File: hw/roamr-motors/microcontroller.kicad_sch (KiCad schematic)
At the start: 38 parts, among them J1 USB_C_Receptacle_USB2.0_14P, J2 USB_C_Receptacle_USB2.0_14P, Q1 L8050QLT1G, Q2 QL8050QLT1G, SW1 SW_MEC_5G, SW2 SW_MEC_5G, U3 ESP32-S3-WROOM-1, U4 CP2102N-A02-GQFN28

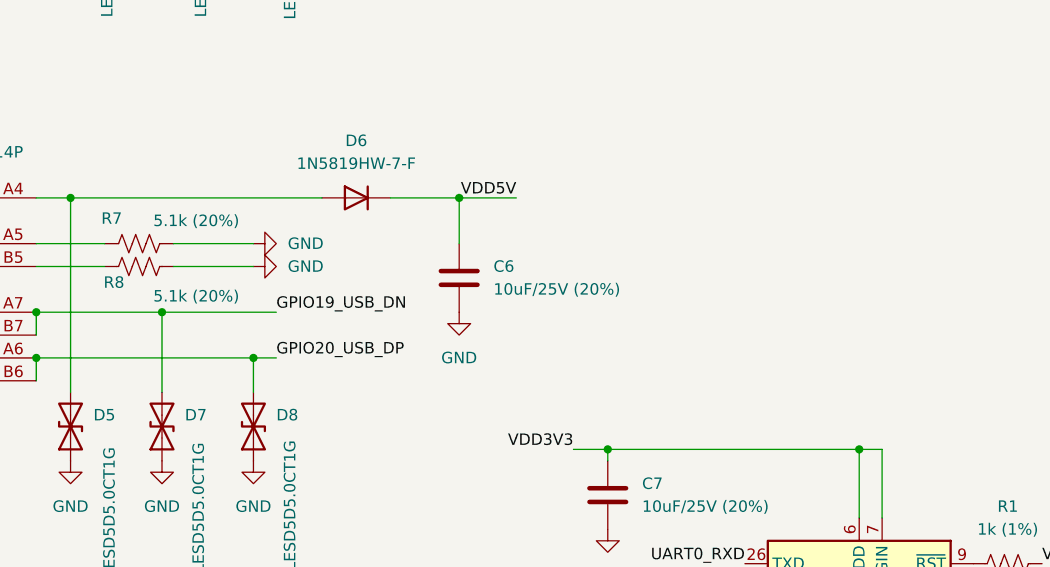
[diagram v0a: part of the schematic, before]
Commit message: Add series resistors
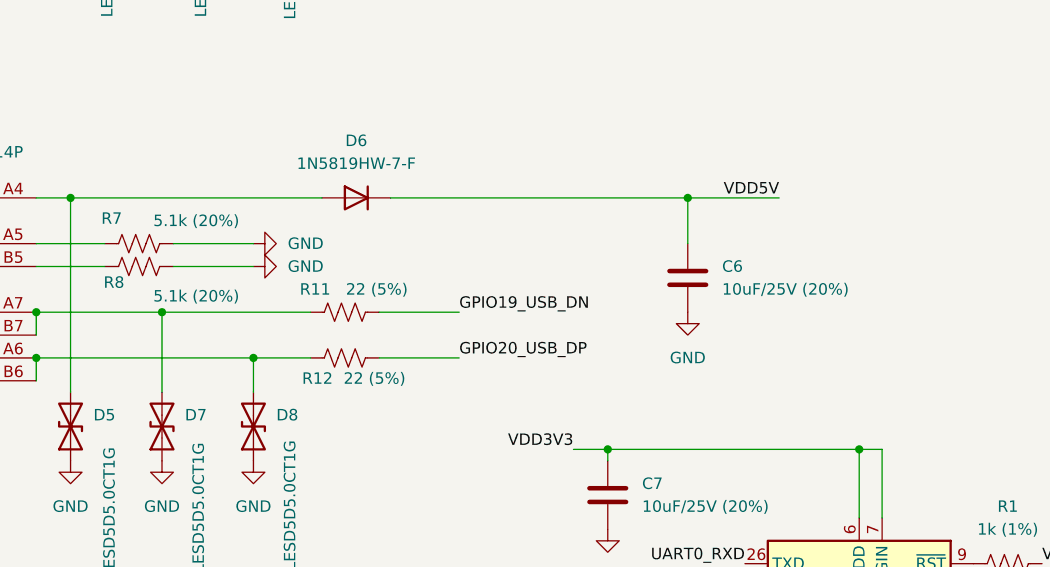
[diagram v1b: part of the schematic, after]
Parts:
- added R11, R12: 22 (5%), symbol Device:R_US
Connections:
- net GPIO19_USB_DN: now also R11.2; no longer D7.2 (A2), J2.A7 (D-), J2.B7 (D-)
- net GPIO20_USB_DP: now also R12.2; no longer D8.2 (A2), J2.A6 (D+), J2.B6 (D+)
- new net: D8.2 (A2), J2.A6 (D+), J2.B6 (D+), R12.1
- new net: D7.2 (A2), J2.A7 (D-), J2.B7 (D-), R11.1
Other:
- moved on the sheet: C6
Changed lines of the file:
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@@
 	)
 	(junction
-		(at 71.12 102.87)
-		(diameter 0)
-		(color 0 0 0 0)
-	)
-	(junction
 		(at 170.18 138.43)
 		(diameter 0)
@@
 	)
 	(junction
-		(at 60.96 97.79)
-		(diameter 0)
-		(color 0 0 0 0)
-	)
-	(junction
-		(at 93.98 85.09)
-		(diameter 0)
-		(color 0 0 0 0)
-	)
-	(junction
 		(at 71.12 41.91)
 		(diameter 0)
@@
 	)
 	(junction
+		(at 60.96 97.79)
+		(diameter 0)
+		(color 0 0 0 0)
+	)
+	(junction
 		(at 50.8 24.13)
 		(diameter 0)
@@
 		(color 0 0 0 0)
 	)
+	(junction
+		(at 119.38 85.09)
+		(diameter 0)
+		(color 0 0 0 0)
+	)
+	(junction
+		(at 71.12 102.87)
+		(diameter 0)
+		(color 0 0 0 0)
+	)
 	(no_connect
 		(at 125.73 181.61)
@@
 	(wire
 		(pts
-			(xy 71.12 102.87) (xy 73.66 102.87)
-		)
-		(stroke
-			(width 0)
-			(type default)
-		)
-	)
-	(wire
-		(pts
 			(xy 46.99 97.79) (xy 46.99 100.33)
 		)
@@
 	(wire
 		(pts
-			(xy 100.33 85.09) (xy 93.98 85.09)
-		)
-		(stroke
-			(width 0)
-			(type default)
-		)
-	)
-	(wire
-		(pts
 			(xy 187.96 138.43) (xy 196.85 138.43)
 		)
@@
 	(wire
 		(pts
+			(xy 86.36 85.09) (xy 119.38 85.09)
+		)
+		(stroke
+			(width 0)
+			(type default)
+		)
+	)
+	(wire
+		(pts
+			(xy 85.09 97.79) (xy 93.98 97.79)
+		)
+		(stroke
+			(width 0)
+			(type default)
+		)
+	)
+	(wire
+		(pts
 			(xy 119.38 26.67) (xy 121.92 26.67)
 		)
@@
 	(wire
 		(pts
-			(xy 100.33 24.13) (xy 93.98 24.13)
+			(xy 71.12 102.87) (xy 77.47 102.87)
 		)
 		(stroke
@@
 	(wire
 		(pts
-			(xy 60.96 97.79) (xy 73.66 97.79)
+			(xy 100.33 24.13) (xy 93.98 24.13)
 		)
 		(stroke
@@
 	(wire
 		(pts
+			(xy 85.09 102.87) (xy 93.98 102.87)
+		)
+		(stroke
+			(width 0)
+			(type default)
+		)
+	)
+	(wire
+		(pts
 			(xy 170.18 138.43) (xy 187.96 138.43)
 		)
@@
 	(wire
 		(pts
-			(xy 86.36 85.09) (xy 93.98 85.09)
+			(xy 200.66 104.14) (xy 205.74 104.14)
 		)
 		(stroke
@@
 	(wire
 		(pts
-			(xy 200.66 104.14) (xy 205.74 104.14)
+			(xy 60.96 97.79) (xy 77.47 97.79)
 		)
 		(stroke
@@
 	(wire
 		(pts
+			(xy 129.54 85.09) (xy 119.38 85.09)
+		)
+		(stroke
+			(width 0)
+			(type default)
+		)
+	)
+	(wire
+		(pts
 			(xy 140.97 113.03) (xy 140.97 120.65)
 		)
@@
 	(wire
 		(pts
-			(xy 93.98 90.17) (xy 93.98 85.09)
+			(xy 119.38 90.17) (xy 119.38 85.09)
 		)
 		(stroke
@@
 	)
 	(label "GPIO19_USB_DN"
-		(at 73.66 97.79 0)
+		(at 93.98 97.79 0)
 		(effects
 			(font
@@
 	)
 	(label "VDD5V"
-		(at 100.33 85.09 180)
+		(at 129.54 85.09 180)
 		(effects
 			(font
@@
 	)
 	(label "GPIO20_USB_DP"
-		(at 73.66 102.87 0)
+		(at 93.98 102.87 0)
 		(effects
 			(font
@@
 	)
 	(symbol
+		(lib_id "Device:R_US")
+		(at 81.28 102.87 90)
+		(unit 1)
+		(exclude_from_sim no)
+		(in_bom yes)
+		(on_board yes)
+		(dnp no)
+		(property "Reference" "R12"
+			(at 78.232 105.156 90)
+			(effects
+				(font
+					(size 1.27 1.27)
+				)
+			)
+		)
+		(property "Value" "22 (5%)"
+			(at 84.582 105.156 90)
+			(effects
+				(font
+					(size 1.27 1.27)
+				)
+			)
+		)
+		(property "Footprint" ""
+			(at 81.534 101.854 90)
+			(effects
+				(font
+					(size 1.27 1.27)
+				)
+				(hide yes)
+			)
+		)
+		(property "Datasheet" "~"
+			(at 81.28 102.87 0)
+			(effects
+				(font
+					(size 1.27 1.27)
+				)
+				(hide yes)
+			)
+		)
+		(property "Description" "Resistor, US symbol"
+			(at 81.28 102.87 0)
+			(effects
+				(font
+					(size 1.27 1.27)
+				)
+				(hide yes)
+			)
+		)
+		(pin "2"
+		)
+		(pin "1"
+		)
+		(instances
+			(project "roamr-motors"
+				(path "/db664d1d-d972-4e66-af85-94b6971e1c6e/206ea9a6-1e38-4e76-a070-d60887d5750e"
+					(reference "R12")
+					(unit 1)
+				)
+			)
+		)
+	)
+	(symbol
+		(lib_id "Device:R_US")
+		(at 81.28 97.79 90)
+		(unit 1)
+		(exclude_from_sim no)
+		(in_bom yes)
+		(on_board yes)
+		(dnp no)
+		(property "Reference" "R11"
+			(at 77.978 95.25 90)
+			(effects
+				(font
+					(size 1.27 1.27)
+				)
+			)
+		)
+		(property "Value" "22 (5%)"
+			(at 84.836 95.25 90)
+			(effects
+				(font
+					(size 1.27 1.27)
+				)
+			)
+		)
+		(property "Footprint" ""
+			(at 81.534 96.774 90)
+			(effects
+				(font
+					(size 1.27 1.27)
+				)
+				(hide yes)
+			)
+		)
+		(property "Datasheet" "~"
+			(at 81.28 97.79 0)
+			(effects
+				(font
+					(size 1.27 1.27)
+				)
+				(hide yes)
+			)
+		)
+		(property "Description" "Resistor, US symbol"
+			(at 81.28 97.79 0)
+			(effects
+				(font
+					(size 1.27 1.27)
+				)
+				(hide yes)
+			)
+		)
+		(pin "1"
+		)
+		(pin "2"
+		)
+		(instances
+			(project "roamr-motors"
+				(path "/db664d1d-d972-4e66-af85-94b6971e1c6e/206ea9a6-1e38-4e76-a070-d60887d5750e"
+					(reference "R11")
+					(unit 1)
+				)
+			)
+		)
+	)
+	(symbol
 		(lib_id "power:GND")
 		(at 60.96 53.34 0)
@@
 	(symbol
 		(lib_id "power:GND")
-		(at 93.98 97.79 0)
+		(at 119.38 97.79 0)
 		(unit 1)
 		(exclude_from_sim no)
@@
 		(fields_autoplaced yes)
 		(property "Reference" "#PWR015"
-			(at 93.98 104.14 0)
+			(at 119.38 104.14 0)
 			(effects
 				(font
@@
 		)
 		(property "Value" "GND"
-			(at 93.98 102.87 0)
+			(at 119.38 102.87 0)
 			(effects
 				(font
@@
 		)
 		(property "Footprint" ""
-			(at 93.98 97.79 0)
+			(at 119.38 97.79 0)
 			(effects
 				(font
@@
 		)
 		(property "Datasheet" ""
-			(at 93.98 97.79 0)
+			(at 119.38 97.79 0)
 			(effects
 				(font
@@
 		)
 		(property "Description" "Power symbol creates a global label with name \"GND\" , ground"
-			(at 93.98 97.79 0)
+			(at 119.38 97.79 0)
 			(effects
 				(font
@@
 	(symbol
 		(lib_id "Device:C")
-		(at 93.98 93.98 0)
+		(at 119.38 93.98 0)
 		(unit 1)
 		(exclude_from_sim no)
@@
 		(fields_autoplaced yes)
 		(property "Reference" "C6"
-			(at 97.79 92.7099 0)
+			(at 123.19 92.7099 0)
 			(effects
 				(font
@@
 		)
 		(property "Value" "10uF/25V (20%)"
-			(at 97.79 95.2499 0)
+			(at 123.19 95.2499 0)
 			(effects
 				(font
@@
 		)
 		(property "Footprint" ""
-			(at 94.9452 97.79 0)
+			(at 120.3452 97.79 0)
 			(effects
 				(font
@@
 		)
 		(property "Datasheet" "~"
-			(at 93.98 93.98 0)
+			(at 119.38 93.98 0)
 			(effects
 				(font
@@
 		)
 		(property "Description" "Unpolarized capacitor"
-			(at 93.98 93.98 0)
+			(at 119.38 93.98 0)
 			(effects
 				(font

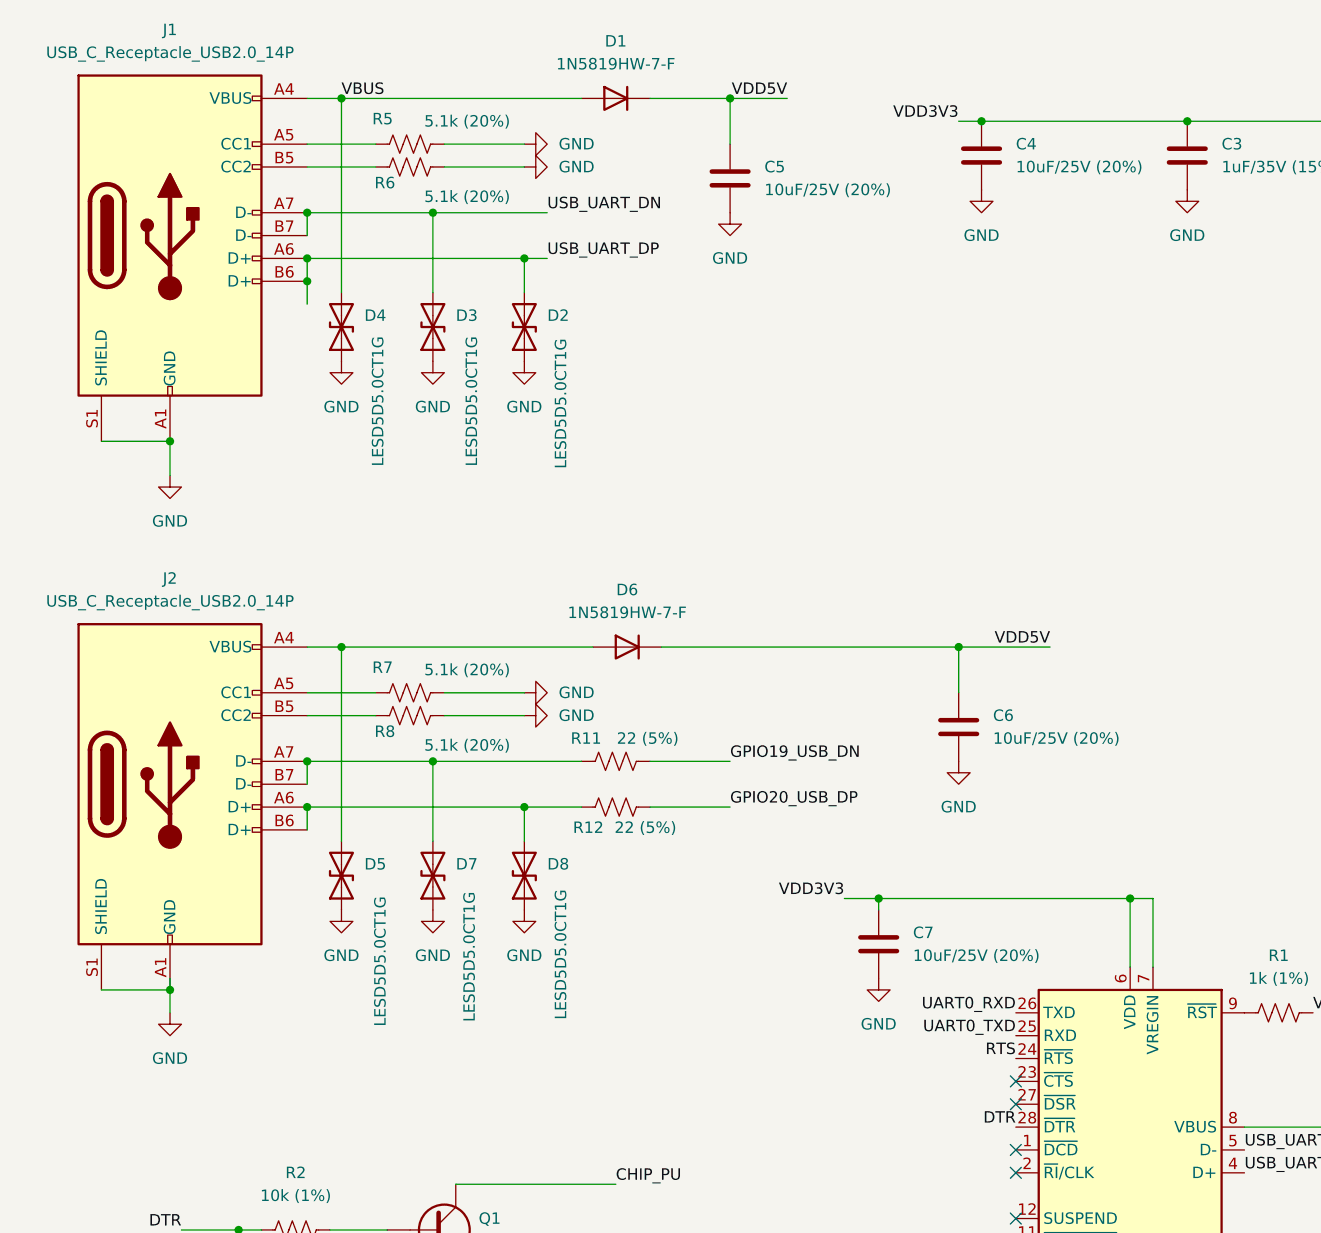
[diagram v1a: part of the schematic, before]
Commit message: just moving around the usb connectors
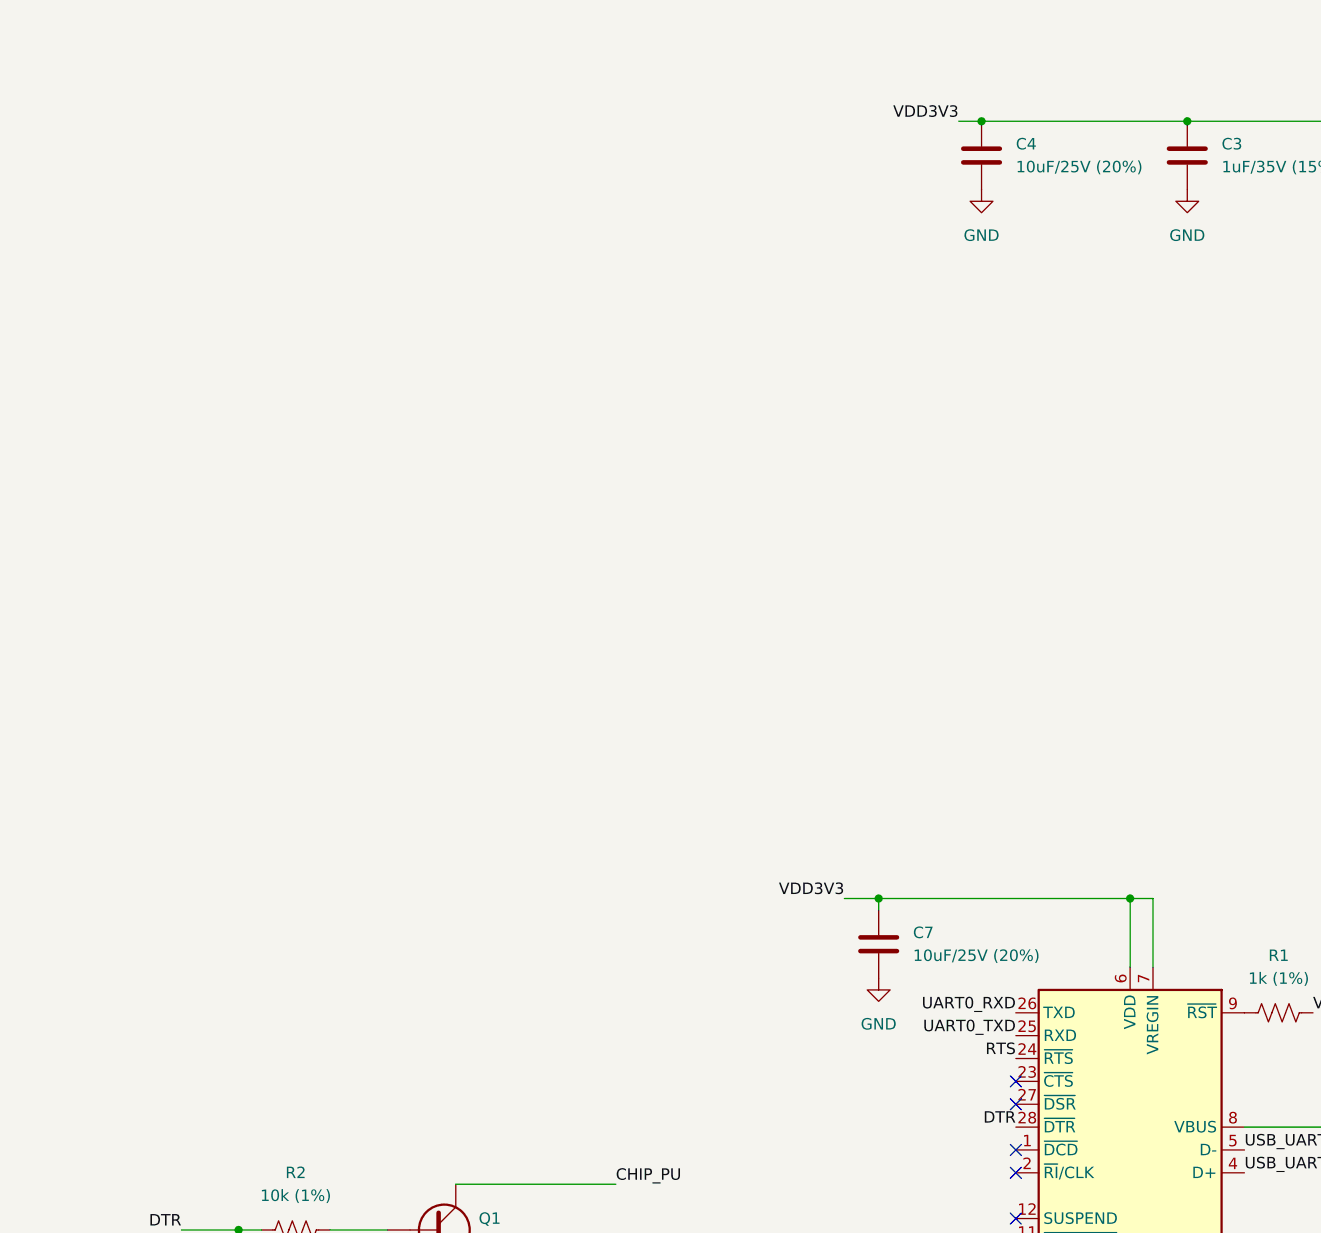
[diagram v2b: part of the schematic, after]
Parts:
- removed C5, C6: 10uF/25V (20%), symbol Device:C
- removed D1, D6: 1N5819HW-7-F, symbol Device:D
- removed D2, D3, D4, D5, D7, D8: LESD5D5.0CT1G, symbol Device:D_TVS
- removed J1, J2: USB_C_Receptacle_USB2.0_14P, symbol Connector:USB_C_Receptacle_USB2.0_14P
- removed R11, R12: 22 (5%), symbol Device:R_US
- removed R5, R6, R7, R8: 5.1k (20%), symbol Device:R_US
